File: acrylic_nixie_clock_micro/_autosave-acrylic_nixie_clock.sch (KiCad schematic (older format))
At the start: 23 parts, among them IC1 OPT3001DNPR, J1 USB_B_Micro, J2 AVR-ISP-6, Q1 S9013, U1 ATmega328P-AU, U2 AMS1117-3.3v, U3 RX-8025T-UB, Y1 X322516MLB4SI

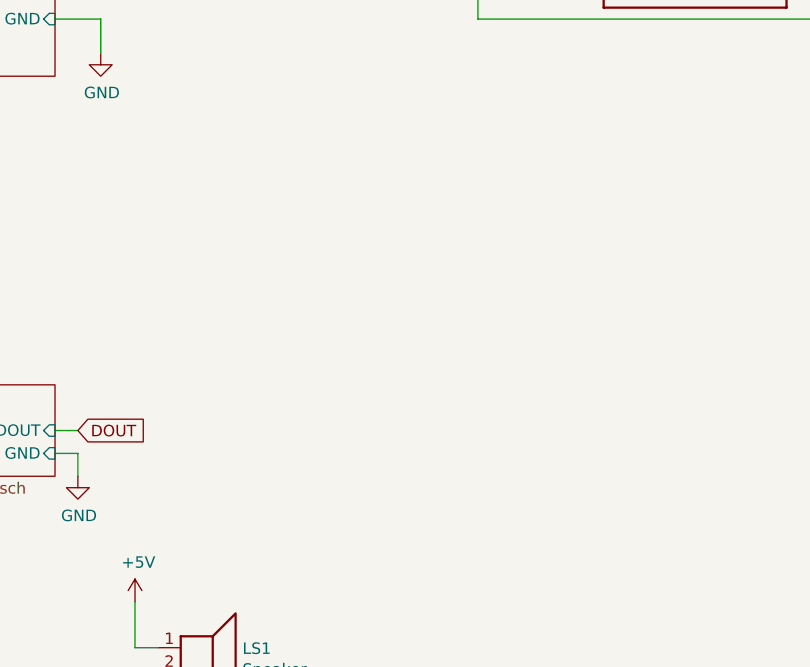
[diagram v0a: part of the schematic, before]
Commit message: 問題点を修正
CH304Gの電源電圧を3.3Vに
RSTにコンデンサを追加
USBのフットプリントを修正
カードコネクタの追加
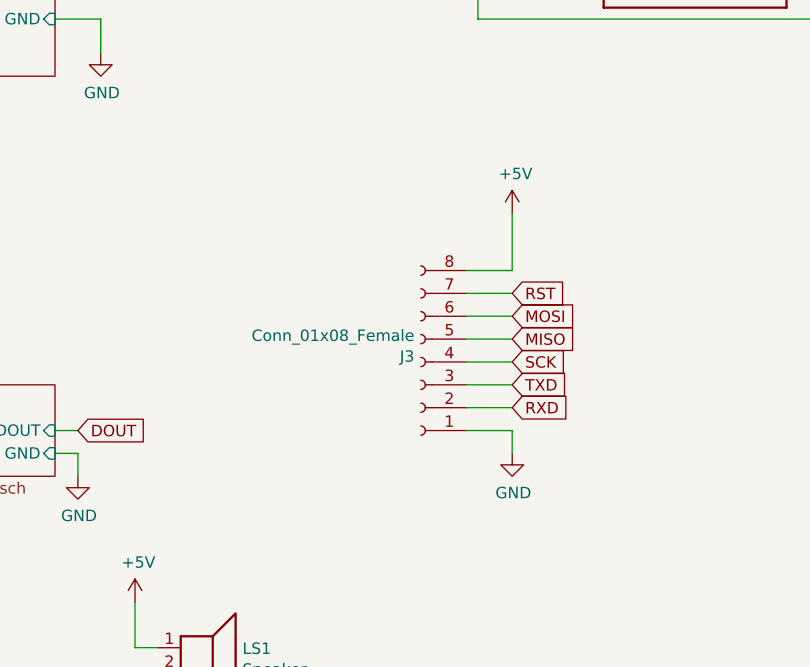
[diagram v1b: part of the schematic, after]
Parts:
- added J3: Conn_01x08_Female, write_card:writer_card, symbol Connector:Conn_01x08_Female
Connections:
- net +5V: now also J3.8 (Pin_8)
- net GND: now also J3.1 (Pin_1)
- net MISO: now also J3.5 (Pin_5)
- net MOSI: now also J3.6 (Pin_6)
- net RST: now also J3.7 (Pin_7)
- net RXD: now also J3.2 (Pin_2)
- net SCK: now also J3.4 (Pin_4)
- net TXD: now also J3.3 (Pin_3)
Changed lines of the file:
@@
 	0    1    1    0
 $EndComp
+$Comp
+L Connector:Conn_01x08_Female J3
+U 1 1 5F83466F
+P 8250 3450
+F 0 "J3" H 8278 3426 50  0000 L CNN
+F 1 "Conn_01x08_Female" H 8278 3335 50  0000 L CNN
+F 2 "write_card:writer_card" H 8250 3450 50  0001 C CNN
+F 3 "~" H 8250 3450 50  0001 C CNN
+	1    8250 3450
+	-1   0    0    1
+$EndComp
+$Comp
+L power:GND #PWR?
+U 1 1 5F83748C
+P 8650 3850
+AR Path="/5E92CCE6/5F83748C" Ref="#PWR?"  Part="1"
+AR Path="/5F83748C" Ref="#PWR026"  Part="1"
+AR Path="/5EA17FAE/5F83748C" Ref="#PWR?"  Part="1"
+AR Path="/5FA639E8/5F83748C" Ref="#PWR?"  Part="1"
+F 0 "#PWR026" H 8650 3600 50  0001 C CNN
+F 1 "GND" H 8655 3677 50  0000 C CNN
+F 2 "" H 8650 3850 50  0001 C CNN
+F 3 "" H 8650 3850 50  0001 C CNN
+	1    8650 3850
+	1    0    0    -1
+$EndComp
+Wire Wire Line
+	8650 3750 8650 3850
+Text GLabel 8650 3150 2    50   Input ~ 0
+RST
+Wire Wire Line
+	8650 2800 8650 3050
+$Comp
+L power:+5V #PWR025
+U 1 1 5F8628DB
+P 8650 2800
+F 0 "#PWR025" H 8650 2650 50  0001 C CNN
+F 1 "+5V" H 8665 2973 50  0000 C CNN
+F 2 "" H 8650 2800 50  0001 C CNN
+F 3 "" H 8650 2800 50  0001 C CNN
+	1    8650 2800
+	1    0    0    -1
+$EndComp
+Text GLabel 8650 3450 2    50   Input ~ 0
+SCK
+Text GLabel 8650 3350 2    50   Input ~ 0
+MISO
+Text GLabel 8650 3250 2    50   Input ~ 0
+MOSI
+Text GLabel 8650 3650 2    50   Input ~ 0
+RXD
+Text GLabel 8650 3550 2    50   Input ~ 0
+TXD
+Wire Wire Line
+	8650 3150 8450 3150
+Wire Wire Line
+	8450 3250 8650 3250
+Wire Wire Line
+	8650 3350 8450 3350
+Wire Wire Line
+	8450 3450 8650 3450
+Wire Wire Line
+	8650 3550 8450 3550
+Wire Wire Line
+	8450 3650 8650 3650
+Wire Wire Line
+	8650 3750 8450 3750
+Wire Wire Line
+	8450 3050 8650 3050
 $EndSCHEMATC
